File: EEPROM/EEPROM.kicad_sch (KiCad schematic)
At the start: 2 parts, among them U27 24LC256

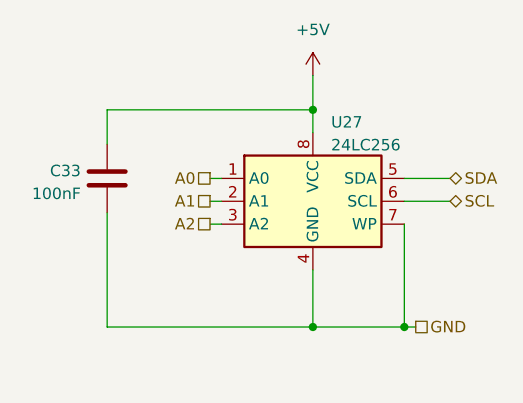
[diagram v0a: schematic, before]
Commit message: moved some schematic scheets to their own folders and routed a board with it. This allow for re-use of PCB parts.
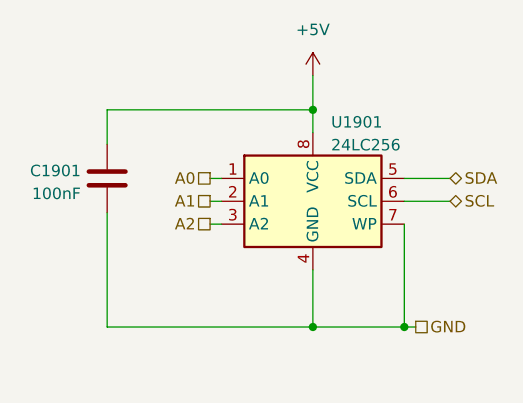
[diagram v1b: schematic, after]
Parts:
- C1901: renamed from C33; footprint Capacitor_SMD:C_0603_1608Metric_Pad1.08x0.95mm_HandSolder -> Capacitor_SMD:C_0603_1608Metric
- renumbered U27 to U1901
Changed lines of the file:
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@@
   (symbol (lib_id "power:+5V") (at 107.95 72.39 0) (unit 1)
     (in_bom yes) (on_board yes) (dnp no) (fields_autoplaced)
-    (property "Reference" "#PWR055" (at 107.95 76.2 0)
+    (property "Reference" "#PWR0154" (at 107.95 76.2 0)
       (effects (font (size 1.27 1.27)) hide)
     )
@@
     (pin "1")
     (instances
+      (project "EEPROM"
+        (path "/7726f3b0-6d28-4a62-ae77-022bfbf3ad3f"
+          (reference "#PWR0801") (unit 1)
+        )
+      )
       (project "general_schematics"
         (path "/e777d9ec-d073-4229-a9e6-2cf85636e407/061d5b60-6a9d-4005-baf0-f56c3f730e99"
-          (reference "#PWR055") (unit 1)
+          (reference "#PWR0154") (unit 1)
         )
       )
@@
   (symbol (lib_id "Memory_EEPROM:24LC256") (at 107.95 86.36 0) (unit 1)
     (in_bom yes) (on_board yes) (dnp no) (fields_autoplaced)
-    (property "Reference" "U27" (at 109.9694 77.5802 0)
+    (property "Reference" "U1901" (at 109.9694 77.5802 0)
       (effects (font (size 1.27 1.27)) (justify left))
     )
@@
     (pin "8")
     (instances
+      (project "EEPROM"
+        (path "/7726f3b0-6d28-4a62-ae77-022bfbf3ad3f"
+          (reference "U801") (unit 1)
+        )
+      )
       (project "general_schematics"
         (path "/e777d9ec-d073-4229-a9e6-2cf85636e407/061d5b60-6a9d-4005-baf0-f56c3f730e99"
-          (reference "U27") (unit 1)
+          (reference "U1901") (unit 1)
         )
       )
@@
   (symbol (lib_id "Device:C") (at 85.09 83.82 0) (mirror x) (unit 1)
     (in_bom yes) (on_board yes) (dnp no) (fields_autoplaced)
-    (property "Reference" "C33" (at 82.169 82.9853 0)
+    (property "Reference" "C1901" (at 82.169 82.9853 0)
       (effects (font (size 1.27 1.27)) (justify right))
     )
@@
       (effects (font (size 1.27 1.27)) (justify right))
     )
-    (property "Footprint" "Capacitor_SMD:C_0603_1608Metric_Pad1.08x0.95mm_HandSolder" (at 86.0552 80.01 0)
+    (property "Footprint" "Capacitor_SMD:C_0603_1608Metric" (at 86.0552 80.01 0)
       (effects (font (size 1.27 1.27)) hide)
     )
@@
     (pin "2")
     (instances
+      (project "EEPROM"
+        (path "/7726f3b0-6d28-4a62-ae77-022bfbf3ad3f"
+          (reference "C801") (unit 1)
+        )
+      )
       (project "general_schematics"
         (path "/e777d9ec-d073-4229-a9e6-2cf85636e407/061d5b60-6a9d-4005-baf0-f56c3f730e99"
-          (reference "C33") (unit 1)
+          (reference "C1901") (unit 1)
         )
       )
     )
   )
+  (sheet_instances
+    (path "/" (page "1"))
+  )
 )

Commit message: added 12V boost converter (300mA max!)
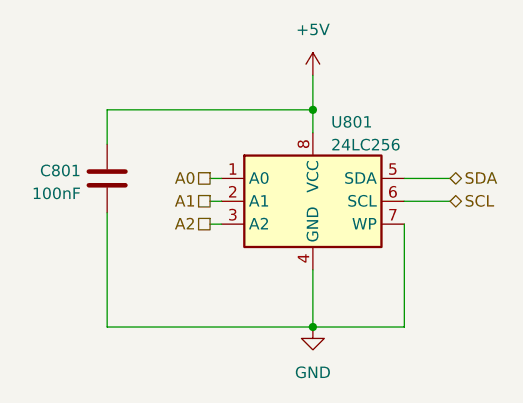
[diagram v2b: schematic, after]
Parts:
- renumbered C1901 to C801, U1901 to U801
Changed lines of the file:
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@@
 (kicad_sch (version 20230121) (generator eeschema)
   (paper "A4")
-  (junction (at 118.11 100.33) (diameter 0) (color 0 0 0 0)
-  )
   (junction (at 107.95 76.2) (diameter 0) (color 0 0 0 0)
   )
@@
     (stroke (width 0) (type default))
   )
-  (wire (pts (xy 118.11 100.33) (xy 119.38 100.33))
-    (stroke (width 0) (type default))
-  )
   (wire (pts (xy 96.52 88.9) (xy 97.79 88.9))
     (stroke (width 0) (type default))
@@
     (effects (font (size 1.27 1.27)) (justify left))
   )
-  (hierarchical_label "GND" (shape passive) (at 119.38 100.33 0) (fields_autoplaced)
-    (effects (font (size 1.27 1.27)) (justify left))
-  )
   (hierarchical_label "A2" (shape passive) (at 96.52 88.9 180) (fields_autoplaced)
     (effects (font (size 1.27 1.27)) (justify right))
@@
   (symbol (lib_id "power:+5V") (at 107.95 72.39 0) (unit 1)
     (in_bom yes) (on_board yes) (dnp no) (fields_autoplaced)
-    (property "Reference" "#PWR0154" (at 107.95 76.2 0)
+    (property "Reference" "#PWR0801" (at 107.95 76.2 0)
       (effects (font (size 1.27 1.27)) hide)
     )
@@
   (symbol (lib_id "Memory_EEPROM:24LC256") (at 107.95 86.36 0) (unit 1)
     (in_bom yes) (on_board yes) (dnp no) (fields_autoplaced)
-    (property "Reference" "U1901" (at 109.9694 77.5802 0)
+    (property "Reference" "U801" (at 109.9694 77.5802 0)
       (effects (font (size 1.27 1.27)) (justify left))
     )
@@
   (symbol (lib_id "Device:C") (at 85.09 83.82 0) (mirror x) (unit 1)
     (in_bom yes) (on_board yes) (dnp no) (fields_autoplaced)
-    (property "Reference" "C1901" (at 82.169 82.9853 0)
+    (property "Reference" "C801" (at 82.169 82.9853 0)
       (effects (font (size 1.27 1.27)) (justify right))
     )
@@
         )
       )
+    )
+  )
+  (symbol (lib_id "power:GND") (at 107.95 100.33 0) (unit 1)
+    (in_bom yes) (on_board yes) (dnp no) (fields_autoplaced)
+    (property "Reference" "#PWR0101" (at 107.95 106.68 0)
+      (effects (font (size 1.27 1.27)) hide)
+    )
+    (property "Value" "GND" (at 107.95 105.41 0)
+      (effects (font (size 1.27 1.27)))
+    )
+    (property "Footprint" "" (at 107.95 100.33 0)
+      (effects (font (size 1.27 1.27)) hide)
+    )
+    (property "Datasheet" "" (at 107.95 100.33 0)
+      (effects (font (size 1.27 1.27)) hide)
+    )
+    (pin "1")
+    (instances
+      (project "EEPROM"
+        (path "/7726f3b0-6d28-4a62-ae77-022bfbf3ad3f"
+          (reference "#PWR0101") (unit 1)
+        )
+      )
